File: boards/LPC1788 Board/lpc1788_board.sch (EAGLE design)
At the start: 99 parts, among them J1 5VDC, J10 MOLEX_527930570_5PIN_FFC_CONN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, J11 20PIN_10X2_.100IN, J12 DF12B-50DX_25X2_0.5MM, J2 SAMTEC_MUSB, J3 JST_2MM_SMT, J4 Console, J5 SMA-J-P-X-ST-EM1, J6 JTAG, J8 NHD-4.3-480272EF, J9 DF12B-50DX_25X2_0.5MM, Q1 MMBT2907, SW1 Reset, SW2 OS102011MA1QS1, U1 LTC3127EMSEPBF, U2 MAX1551EZK+T, U3 LT3497EDDBTRMPBF, U4 CY62167_16MBIT_SRAM, U5 S25FL064P, U6 AR1021-RESISTIVE_TOUCH_CONTRO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, Y1 12MHz

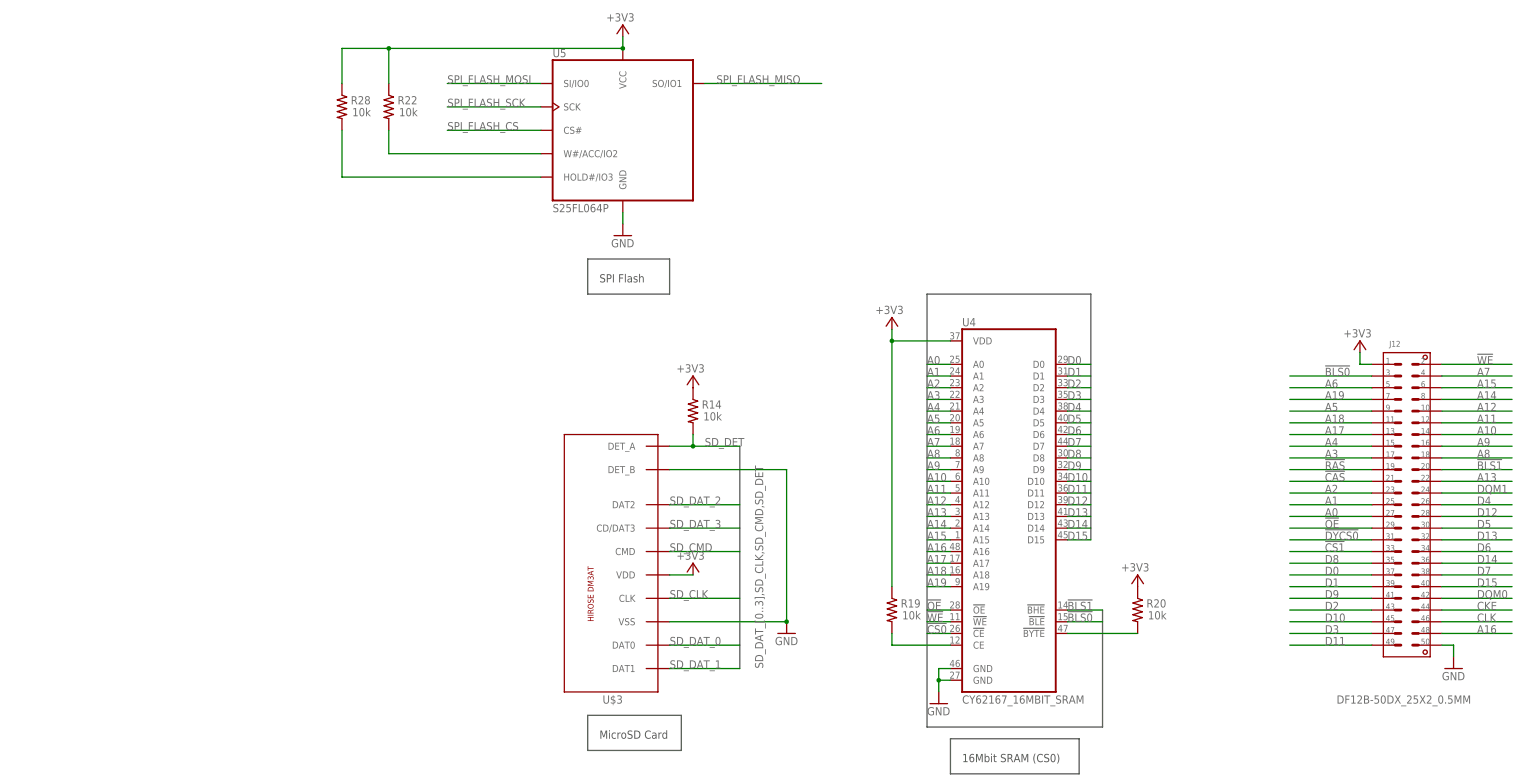
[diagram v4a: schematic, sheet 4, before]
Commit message: switch to sdram
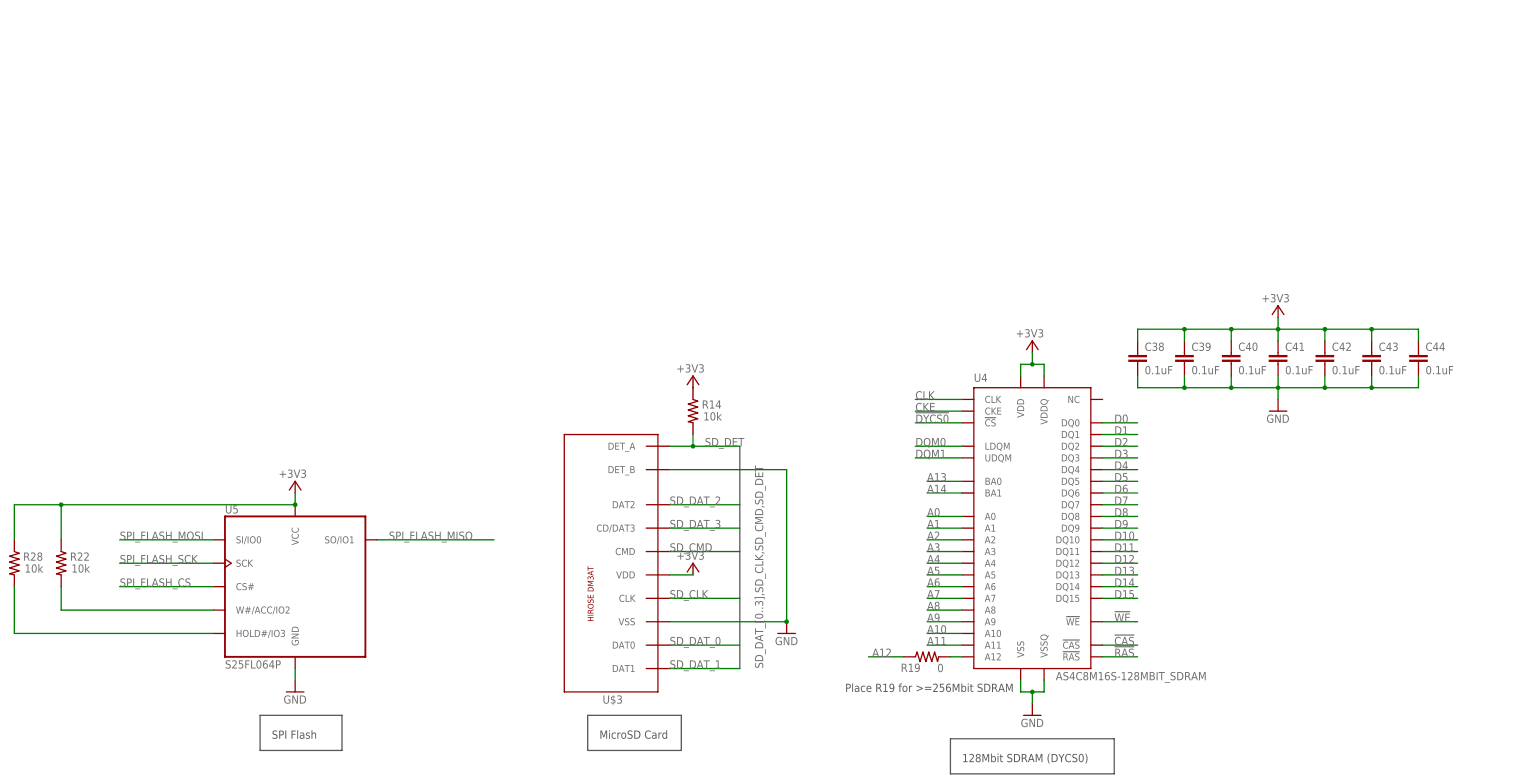
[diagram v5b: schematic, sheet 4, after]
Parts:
- removed J12: DF12B-50DX_25X2_0.5MM, Custom:DF12B-50DX_25X2_0.5MM
- added C38, C39, C40, C41, C42, C43, C44: 0.1uF, rcl:C-EUC0402
- added L6: 470nH, Custom:INDUCTOR_0603
- added R32: 24K, rcl:R-US_R0603
- added R33: 39K, rcl:R-US_R0603
- R19: value 10k -> 0
- R20: value 10k -> 22
- U4: value CY62167_16MBIT_SRAM -> AS4C8M16S-128MBIT_SDRAM; device Custom:CY62167_16MBIT_SRAM -> Custom:AS4C8M16S-128MBIT_SDRAM
- renumbered U$1 to U7, U$4 to U8
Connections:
- removed net !BLS0: J12.S3, U4.!BLE, U7PORT4.P4[26]/!EMC_BLS0!
- removed net !BLS1: J12.S20, U4.!BHE, U7PORT4.P4[27]/!EMC_BLS1!
- removed net !CS0: U4.!CE, U7PORT4.P4[30]/!EMC_CS0!
- removed net !CS1: J12.S33, U7PORT4.P4[31]/!EMC_CS1!
- removed net !OE: J12.S29, U4.!OE, U7PORT4.P4[24]/!EMC_OE!
- removed net A15: J12.S6, U4.A15, U7PORT4.P4[15]/EMC_A[15]
- removed net A16: J12.S48, U4.A16, U7PORT4.P4[16]/EMC_A[16]
- removed net A17: J12.S13, U4.A17, U7PORT4.P4[17]/EMC_A[17]
- removed net A18: J12.S11, U4.A18, U7PORT4.P4[18]/EMC_A[18]
- removed net A19: J12.S7, U4.A19, U7PORT4.P4[19]/EMC_A[19]
- new net N$42: R32.2, U7PORT1.P1[30]/USB_PWRD2/USB_VBUS/ADC0_IN[4]/I2C0_SDA/U3_OE
- new net N$43: J2.1, L6.1
- net !CAS: now also U4.!CAS; no longer J12.S21
- net !DYCS0: now also U4.!CS; no longer J12.S31
- net !RAS: now also U4.!RAS; no longer J12.S19
- net !WE: no longer J12.S2
- net +3V3: now also C38.1, C39.1, C40.1, C41.1, C42.1, C43.1, C44.1, U4.VDD, U4.VDDQ; no longer J12.S1, R19.1, R20.1, U4.VDD@1
- net +VUSB: now also L6.2, R32.1, R33.1; no longer J2.1
- net A0: no longer J12.S27
- net A1: no longer J12.S25
- net A10: no longer J12.S14
- net A11: no longer J12.S12
- net A12: now also R19.1; no longer J12.S10, U4.A12
- net A13: now also U4.BA0; no longer J12.S22, U4.A13
- net A14: now also U4.BA1; no longer J12.S8, U4.A14
- net A2: no longer J12.S23
- net A3: no longer J12.S17
- net A4: no longer J12.S15
- net A5: no longer J12.S9
- net A6: no longer J12.S5
- net A7: no longer J12.S4
- net A8: no longer J12.S18
- net A9: no longer J12.S16
- net CKE: now also U4.CKE; no longer J12.S44
- net CLK: now also U4.CLK; no longer J12.S46
- net D0: now also U4.DQ0; no longer J12.S37, U4.D0
- net D1: now also U4.DQ1; no longer J12.S39, U4.D1
- net D10: now also U4.DQ10; no longer J12.S45, U4.D10
- net D11: now also U4.DQ11; no longer J12.S49, U4.D11
- net D12: now also U4.DQ12; no longer J12.S28, U4.D12
- net D13: now also U4.DQ13; no longer J12.S32, U4.D13
- net D14: now also U4.DQ14; no longer J12.S36, U4.D14
- net D15: now also U4.DQ15; no longer J12.S40, U4.D15
- net D2: now also U4.DQ2; no longer J12.S43, U4.D2
- net D3: now also U4.DQ3; no longer J12.S47, U4.D3
- net D4: now also U4.DQ4; no longer J12.S26, U4.D4
- net D5: now also U4.DQ5; no longer J12.S30, U4.D5
- net D6: now also U4.DQ6; no longer J12.S34, U4.D6
- net D7: now also U4.DQ7; no longer J12.S38, U4.D7
- net D8: now also U4.DQ8; no longer J12.S35, U4.D8
- net D9: now also U4.DQ9; no longer J12.S41, U4.D9
- net DQM0: now also U4.LDQM; no longer J12.S42
- net DQM1: now also U4.UDQM; no longer J12.S24
- net GND: now also C38.2, C39.2, C40.2, C41.2, C42.2, C43.2, C44.2, R33.2, U4.VSS, U4.VSSQ; no longer J12.S50, U4.GND@1, U4.GND@2
- net N$22: now also R20.1; no longer Q1.B
- net N$28: now also U4.A12; no longer U4.CE
- net N$29: now also Q1.B; no longer U4.!BYTE
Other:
- note added: "128Mbit SDRAM (DYCS0)"
- note added: "Add touch control lines to header"
- note added: "Change out these GPIO for easier to route ones"
- note added: "NOTE: To meet USB spec C32/C5 may need to be reduced."
- note added: "NOTE: USB_VUSB connection may not be needed"
- note added: "Place R19 for >=256Mbit SDRAM"
- note removed: "16Mbit SRAM (CS0)"
- moved on the sheet: Q1, R15, R19, R22, R28, U5

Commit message: LPC1788 Board Rev 1
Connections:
- removed net N$30: J11.S13, U7PORT5.P5[4]/U0_OE/T3_MAT3/U4_TXD
- new net GPIO1: J11.S15, U7PORT3.P3[31]/EMC_D[31]/T1_MAT2
- new net GPIO2: J11.S13, U7PORT0.P0[23]/ADC0_IN[0]/I2S_RX_SCK/T3_CAP0
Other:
- note removed: "Add touch control lines to header"
- note removed: "Change out these GPIO for easier to route ones"
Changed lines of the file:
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@@
 <text x="109.22" y="-172.72" size="2.54" layer="97">Expansion Interface</text>
 <text x="330.2" y="22.86" size="1.778" layer="97">NOTE: USB_VUSB connection may not be needed</text>
-<text x="48.26" y="-182.88" size="5.08" layer="97">Change out these GPIO for easier to route ones</text>
 </plain>
 <instances>
@@
 <segment>
 <pinref part="U7" gate="PORT4" pin="P4[25]/!EMC_WE!"/>
-<wire x1="317.5" y1="-86.36" x2="327.66" y2="-86.36" width="0.1524" layer="91"/>
+<wire x1="317.5" y1="-86.36" x2="325.12" y2="-86.36" width="0.1524" layer="91"/>
 <label x="320.04" y="-86.36" size="1.778" layer="95"/>
 </segment>
@@
 <wire x1="154.94" y1="27.94" x2="170.18" y2="27.94" width="0.1524" layer="91"/>
 <label x="157.48" y="27.94" size="1.778" layer="95"/>
-</segment>
-</net>
-<net name="N$30" class="0">
-<segment>
-<pinref part="U7" gate="PORT5" pin="P5[4]/U0_OE/T3_MAT3/U4_TXD"/>
-<wire x1="71.12" y1="-147.32" x2="116.84" y2="-147.32" width="0.1524" layer="91"/>
-<pinref part="J11" gate="G$1" pin="S13"/>
 </segment>
 </net>
@@
 <wire x1="340.36" y1="15.24" x2="340.36" y2="12.7" width="0.1524" layer="91"/>
 <junction x="340.36" y="12.7"/>
+</segment>
+</net>
+<net name="GPIO1" class="0">
+<segment>
+<pinref part="U7" gate="PORT3" pin="P3[31]/EMC_D[31]/T1_MAT2"/>
+<wire x1="195.58" y1="-101.6" x2="210.82" y2="-101.6" width="0.1524" layer="91"/>
+<label x="200.66" y="-101.6" size="1.778" layer="95"/>
+</segment>
+<segment>
+<pinref part="J11" gate="G$1" pin="S15"/>
+<wire x1="116.84" y1="-149.86" x2="106.68" y2="-149.86" width="0.1524" layer="91"/>
+<label x="109.22" y="-149.86" size="1.778" layer="95"/>
+</segment>
+</net>
+<net name="GPIO2" class="0">
+<segment>
+<pinref part="U7" gate="PORT0" pin="P0[23]/ADC0_IN[0]/I2S_RX_SCK/T3_CAP0"/>
+<wire x1="154.94" y1="25.4" x2="167.64" y2="25.4" width="0.1524" layer="91"/>
+<label x="157.48" y="25.4" size="1.778" layer="95"/>
+</segment>
+<segment>
+<pinref part="J11" gate="G$1" pin="S13"/>
+<wire x1="116.84" y1="-147.32" x2="106.68" y2="-147.32" width="0.1524" layer="91"/>
+<label x="109.22" y="-147.32" size="1.778" layer="95"/>
 </segment>
 </net>
@@
 <description>LCD</description>
 <plain>
-<text x="106.68" y="58.42" size="5.08" layer="97">Add touch control lines to header</text>
 </plain>
 <instances>

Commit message: Storing local changes before upgrading to eagle 6.6.0
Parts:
- removed C32: 10uF, rcl:C-EUC0402
- removed C37: 330uF, rcl:C-EUC1206
- removed J1: 5VDC, Custom:DC_POWER_JACK_PJ-045
- removed J8: NHD-4.3-480272EF, Custom:NHD-4.3-480272EF
- removed L3: 15uH, rcl:L-USL3225M
- removed LED1: CHG, led:LEDCHIPLED_0603
- removed SW2: OS102011MA1QS1, Custom:OS102011MA1QS1
- removed U5: S25FL064P, Custom:S25FL064P
- added CHG, PGOOD: USB, led:LEDCHIPLED_0603
- added D1: (no value), Custom:B0540WS-SCHOTTKY_DIODE
- added PWR: OS102011MA1QS1, Custom:OS102011MA1QS1
- added Q3: FDN335N, Custom:FDN335N
- added R34, R36: 10K, rcl:R-US_R0402
- added R35: 2.5, rcl:R-US_R0402
- added SW3: ISP, Custom:SMT_PUSHBUTTON
- added TH1: (no value), rcl:R-EU_0204/2V
- C1: value 10uF -> 18pF
- C10, C3: value 1uF -> 10uF; device rcl:C-EUC0402 -> rcl:C-EUC0805K
- C11, C9: value 1uF -> 10uF; device rcl:C-EUC0805 -> rcl:C-EUC0805K
- C12: value 18pF -> 10uF; device rcl:C-EUC0603 -> rcl:C-EUC0805K
- C13: value 18pF -> 1uF; device rcl:C-EUC0603 -> rcl:C-EUC0402
- C16: value 0.1uF -> 1uF; device rcl:C-EUC0603 -> rcl:C-EUC0402
- C2: value 100pF -> 18pF
- C4: value 22uF -> 0.1uF; device rcl:C-EUC0805 -> rcl:C-EUC0402
- C6: value 100uF -> 0.1uF; device rcl:C-EUC1206 -> rcl:C-EUC0402
- C7: value 1uF -> 0.1uF
- C8: value 330uF -> 10uF; device rcl:C-EUC1206 -> rcl:C-EUC0805K
- L1: value 4.7uH -> 3.3uH; device Custom:INDUCTOR_NR6028 -> Custom:NR3015T3R3M-INDUCTOR
- L2: value 15uH -> 22uH; device rcl:L-USL3225M -> Custom:NR4012T220M
- R1: value 320k -> 100K
- R11: value 100K -> 4.7K; device rcl:R-US_R0603 -> rcl:R-US_R0402
- R12, R26, R27: device rcl:R-US_R0603 -> rcl:R-US_R0402
- R13: value 4.7K -> 1.5K; device rcl:R-US_R0603 -> rcl:R-US_R0402
- R14, R28: value 10k -> 10K
- R15: value 1.5K -> 39K; device rcl:R-US_R0603 -> rcl:R-US_R0402
- R2: value 182k -> 10K
- R22: value 10k -> 24K
- R23: value 10K -> 0; device rcl:R-US_R0603 -> rcl:R-US_R0402
- R24, R25: value 10K -> 1.5K; device rcl:R-US_R0603 -> rcl:R-US_R0402
- R29: value 4.7K -> 3.57K; device rcl:R-US_R0603 -> rcl:R-US_R0402
- R3: value 32.4k -> 10K
- R30: value 4.7K -> 2.94K; device rcl:R-US_R0603 -> rcl:R-US_R0402
- R32: value 24K -> 4.32K; device rcl:R-US_R0603 -> rcl:R-US_R0402
- R33: value 39K -> 56.2K; device rcl:R-US_R0603 -> rcl:R-US_R0402
- R4: value 50 -> 10K
- R5: value 499k -> 10K
- R6: value 10 -> 100K
- R7: value 10 -> 10K
- R8, R9: value 10K -> 4.7K
- U1: value LTC3127EMSEPBF -> BQ24232H-BATTERY_CHARGER; device LTC:LTC3127EMSEPBF -> Custom:BQ24232H-BATTERY_CHARGER
- U2: value MAX1551EZK+T -> TPS63001-BUCK-BOOST_CONVERTER; device Maxim:MAX1551EZK+T -> Custom:TPS63001-BUCK-BOOST_CONVERTER
- U3: value LT3497EDDBTRMPBF -> AP5724; device LTC:LT3497EDDBTRMPBF -> Custom:AP5724
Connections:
- removed net +VBAT: C1.1, C10.1, C37.1, C7.1, L2.1, L3.1, R4.2, R8.2, SW2.S, U1.VIN, U1.~SHDN, U2.BAT, U3.VIN
- removed net LED1_PWR: J8.LED+, J9.S30, J9.S32, R6.1, U3.LED1
- removed net LED2_PWR: J9.S36, J9.S38, R7.1, U3.LED2
- removed net N$20: J3.+, SW2.P
- removed net SPI_FLASH_CS: U5.CS#, U7PORT0.P0[16]/U1_RXD/SSP0_SSEL
- removed net SPI_FLASH_MISO: U5.SO/IO1, U7PORT0.P0[17]/U1_CTS/SSP0_MISO
- removed net SPI_FLASH_MOSI: U5.SI/IO0, U7PORT0.P0[18]/U1_DCD/SSP0_MOSI
- removed net SPI_FLASH_SCK: U5.SCK, U7PORT0.P0[15]/U1_TXD/SSP0_SCK
- removed net V+: C3.1, J1.1, U2.DC
- new net /RESET1: C6.1, R1.1, SW3.P, SW3.P1, U7PORT2.P2[10]/EINT_0/NMI
- new net LED_A: C16.1, D1.C, J9.S30, J9.S32, U3.OVP
- new net LED_K: J9.S36, J9.S38, R35.2, U3.FB
- new net N$10: R34.1, TH1.2, U1.TS
- new net N$14: C10.1, PWR.S, U2.EN, U2.PS/SYNC, U2.VIN, U2.VINA
- new net N$19: R33.2, U1.TMR
- new net N$30: L1.1, U2.L1
- new net N$9: C3.1, J3.+, U1.BAT, U1.BAT@1
- new net SD_PWR: Q3.G, U7PORT0.P0[21]/U1_RI/SD_PWR/U4_OE/CAN_RD1
- net +3V3: now also C11.1, C12.1, C13.1, L2.1, Q3.D, R12.2, R2.2, R3.2, R4.2, R6.2, R7.2, R8.2, R9.2, U2.FB, U2.VOUT, U3.VIN; no longer C4.1, C6.1, C8.1, J8.VDD, R12.1, R13.1, R22.1, R25.1, R26.1, R27.1, R28.1, R29.1, R30.1, U$3.VDD, U1.VOUT, U5.VCC
- net +VUSB: now also R15.2, R22.2, U1.IN; no longer C32.1, R32.1, R33.1, U2.USB
- net /RESET: now also C4.1, R6.1; no longer C16.1, R11.1
- net B0: no longer J8.B0
- net B1: no longer J8.B1
- net B2: no longer J8.B2
- net B3: no longer J8.B3
- net B4: no longer J8.B4
- net B5: no longer J8.B5
- net B6: no longer J8.B6
- net B7: no longer J8.B7
- net G0: no longer J8.G0
- net G1: no longer J8.G1
- net G2: no longer J8.G2
- net G3: no longer J8.G3
- net G4: no longer J8.G4
- net G5: no longer J8.G5
- net G6: no longer J8.G6
- net G7: no longer J8.G7
- net GND: now also R15.1, R27.1, R28.2, R29.1, R30.1, R32.1, R33.1, R34.2, R35.1, R36.1, SW3.S, SW3.S1, TH1.1, U1.!CE, U1.VSS, U2.PGND; no longer C32.2, C37.2, J1.2, J1.3, J8.GND, J8.GND@1, J8.GND@2, J8.LED-, R2.1, R24.2, R3.1, R33.2, R9.1, U1.MODE, U1.PGND, U1.PGND_2, U1.PGND_3, U1.SGND, U3.GND_2, U5.GND
- net KEY_I2C_SCL: now also R11.1; no longer R30.2
- net KEY_I2C_SDA: now also R12.1; no longer R29.2
- net LCD_DCLK: no longer J8.CLK
- net LCD_ENAB_M: no longer J8.DE
- net LCD_FP: no longer J8.VSYNC
- net LCD_LP: no longer J8.HSYNC
- net LCD_PWR: no longer J8.DISP
- net LED_CTRL: now also R36.2, U3.EN; no longer R8.1, R9.2, U3.CTRL1, U3.CTRL2
- net N$1: now also C7.1, C8.1, Q3.S, R23.2, R28.1, U$3.VDD; no longer R3.2, U1.PROG
- net N$11: now also R29.2, U1.ITERM; no longer C11.1, R7.2, U3.CAP2
- net N$12: now also R30.2, U1.ILIM; no longer L2.2, U3.SW1
- net N$13: now also R32.2, U1.ISET; no longer L3.2, U3.SW2
- net N$15: now also C1.1; no longer C12.1
- net N$16: now also C2.1; no longer C13.1
- net N$2: now also C9.1, PWR.P, R24.2, R25.2, R26.1, U1.OUT, U1.OUT@1; no longer R1.1, R2.2, U1.FB
- net N$21: now also R13.2; no longer R15.2
- net N$25: now also U7PORT0.P0[2]/U0_TXD/U3_TXD; no longer U7PORT0.P0[0]/CAN_RD1/U3_TXD/I2C1_SDA/U0_TXD
- net N$26: now also U7PORT0.P0[3]/U0_RXD/U3_RXD; no longer U7PORT0.P0[1]/CAN_TD1/U3_RXD/I2C1_SCL/U0_RXD
- net N$3: now also R26.2, U1.EN2; no longer L1.2, U1.SW1
- net N$31: now also L1.2, U2.L2; no longer R22.2, U5.W#/ACC/IO2
- net N$33: now also D1.A, L2.2, U3.SW; no longer R28.2, U5.HOLD#/IO3
- net N$35: no longer J8.XL
- net N$36: no longer J8.XR
- net N$37: no longer J8.YD
- net N$38: no longer J8.YU
- net N$4: now also R27.2, U1.EN1; no longer L1.1, U1.SW2
- net N$42: now also R22.1; no longer R32.2
- net N$5: now also PGOOD.A, R24.1; no longer LED1.C, U2.~POK
- net N$6: now also CHG.A, R25.1; no longer C9.1, R6.2, U3.CAP1
- net N$7: now also PGOOD.C, U1.!PGOOD; no longer C2.1, R5.2, U1.VC
- net N$8: now also CHG.C, U1.!CHG; no longer LED1.A, R4.1
- net R0: no longer J8.R0
- net R1: no longer J8.R1
- net R2: no longer J8.R2
- net R3: no longer J8.R3
- net R4: no longer J8.R4
- net R5: no longer J8.R5
- net R6: no longer J8.R6
- net R7: no longer J8.R7
- net SCL: now also R8.1; no longer R12.2
- net SDA: now also R9.1; no longer R13.2
- net TCK/SWDCLK: now also R5.2; no longer R24.1
- net TDI: now also R4.1; no longer R26.2
- net TDO/SWO: now also R3.1; no longer R25.2
- net TMS/SWDIO: now also R2.1; no longer R23.2
- net TRST: now also R7.1; no longer R27.2
- net USB_D_P: now also R13.1; no longer R15.1
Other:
- note added: "Place R23 or Q3"
- note removed: "NOTE: To meet USB spec C32/C5 may need to be reduced."
- note removed: "Populate either R8 or R9 R8=Normally On R9=Normally Off"
- note removed: "SPI Flash"

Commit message: updates
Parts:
- removed J11: 20PIN_10X2_.100IN, Custom:20PIN_10X2_.100IN
- removed J5: SMA-J-P-X-ST-EM1, Custom:SMA-J-P-X-ST-EM1
- added 3V3, LED_CTRL, TP1, TP10, TP2, TP3, TP4, TP5, TP6, TP7, TP8, TP9, VSYS, VUSB: TPTP10R, testpad:TPTP10R
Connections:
- removed net N$27: J5.1, U7PORT0.P0[26]/ADC0_IN[3]/DAC_OUT/U3_RXD
- removed net N$32: J11.S7, U7PORT5.P5[1]/EMC_A[25]/T2_MAT3
- removed net N$34: J11.S5, U7PORT5.P5[0]/EMC_A[24]/T2_MAT2
- net +3V3: now also 3V3.TP; no longer J11.S1, J11.S2, J11.S3, J11.S4
- net +VUSB: now also VUSB.TP
- net B0: now also J9.S7; no longer J9.S11
- net B1: now also J9.S9; no longer J9.S13
- net B2: now also J9.S31; no longer J9.S8
- net B3: now also J9.S33; no longer J9.S6
- net B4: now also J9.S41; no longer J9.S37
- net B6: now also J9.S37; no longer J9.S41
- net B7: now also J9.S35; no longer J9.S43
- net EXT_UART_RX: no longer J11.S16
- net EXT_UART_TX: no longer J11.S14
- net G0: now also J9.S18; no longer J9.S15
- net G2: now also J9.S24; no longer J9.S22
- net G3: now also J9.S26; no longer J9.S24
- net G4: now also J9.S40; no longer J9.S16
- net G5: now also J9.S42; no longer J9.S14
- net G6: now also J9.S44; no longer J9.S12
- net G7: now also J9.S46; no longer J9.S10
- net GND: no longer J11.S17, J11.S18, J11.S19, J11.S20, J5.GND
- net GPIO1: no longer J11.S15
- net GPIO2: no longer J11.S13
- net KEY_I2C_SCL: no longer U7PORT5.P5[3]/U4_RXD/I2C0_SCL
- net KEY_I2C_SDA: no longer U7PORT5.P5[2]/T3_MAT2/I2C0_SDA
- net LCD_DCLK: now also J9.S15; no longer J9.S21
- net LCD_ENAB_M: now also J9.S19; no longer J9.S25
- net LCD_FP: now also J9.S17; no longer J9.S23
- net LCD_LE: now also J9.S13; no longer J9.S19
- net LCD_LP: now also J9.S21; no longer J9.S27
- net LCD_PWR: now also J9.S11; no longer J9.S17
- net LED_A: now also J9.S6, J9.S8; no longer J9.S30, J9.S32
- net LED_CTRL: now also LED_CTRL.TP, TP4.TP
- net LED_K: now also J9.S12, J9.S14; no longer J9.S36, J9.S38
- net N$2: now also VSYS.TP
- net N$35: now also J9.S34
- net N$36: now also J9.S32
- net N$37: now also J9.S30
- net N$38: now also J9.S28
- net R0: now also J9.S22; no longer J9.S9
- net R1: now also J9.S20; no longer J9.S7
- net R2: now also J9.S27; no longer J9.S33
- net R3: now also J9.S29; no longer J9.S35
- net R4: now also J9.S23; no longer J9.S29
- net R5: now also J9.S25; no longer J9.S31
- net R6: now also J9.S36; no longer J9.S18
- net R7: now also J9.S38; no longer J9.S20
- net SCL: now also R9.1; no longer J11.S11, R8.1
- net SDA: now also R8.1; no longer J11.S9, R9.1
- net SD_CLK: now also TP1.TP
- net SD_CMD: now also TP2.TP
- net SD_DAT_0: now also TP9.TP
- net SD_DAT_1: now also TP5.TP
- net SD_DAT_2: now also TP7.TP
- net SD_DAT_3: now also TP8.TP
- net SD_PWR: now also TP3.TP
- net SPI_CS: now also TP6.TP; no longer J11.S12
- net SPI_MISO: no longer J11.S10
- net SPI_MOSI: no longer J11.S8
- net SPI_SCK: no longer J11.S6
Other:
- note added: "Place either Q3, R28 or R23"
- note added: "Stuff either TH1 or R34"
- note added: "TODO: Assign pins for KEY I2C fix mounting holes LED_CTRL"
- note removed: "Expansion Interface"
- moved on the sheet: C33, C34, C35, C36, R10, R21, R31, R8, R9, U6, U7PORT3, U7PORT4
